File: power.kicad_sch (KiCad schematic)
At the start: 20 parts, among them U2 BQ25176J, U3 TPS61201DRC

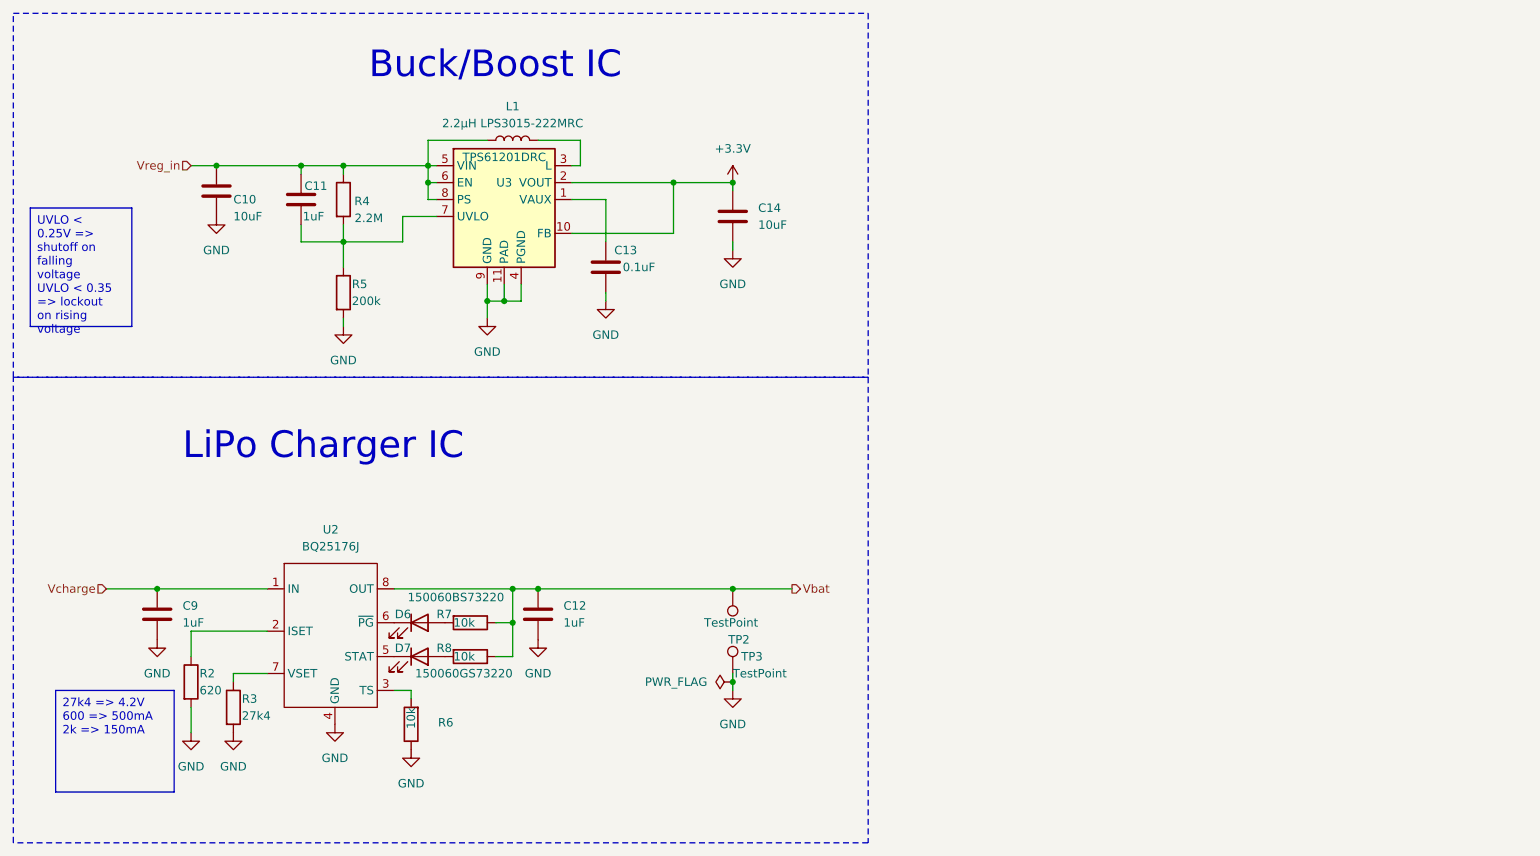
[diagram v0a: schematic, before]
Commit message: update to kicad 9.0 and place Qi-charge IC
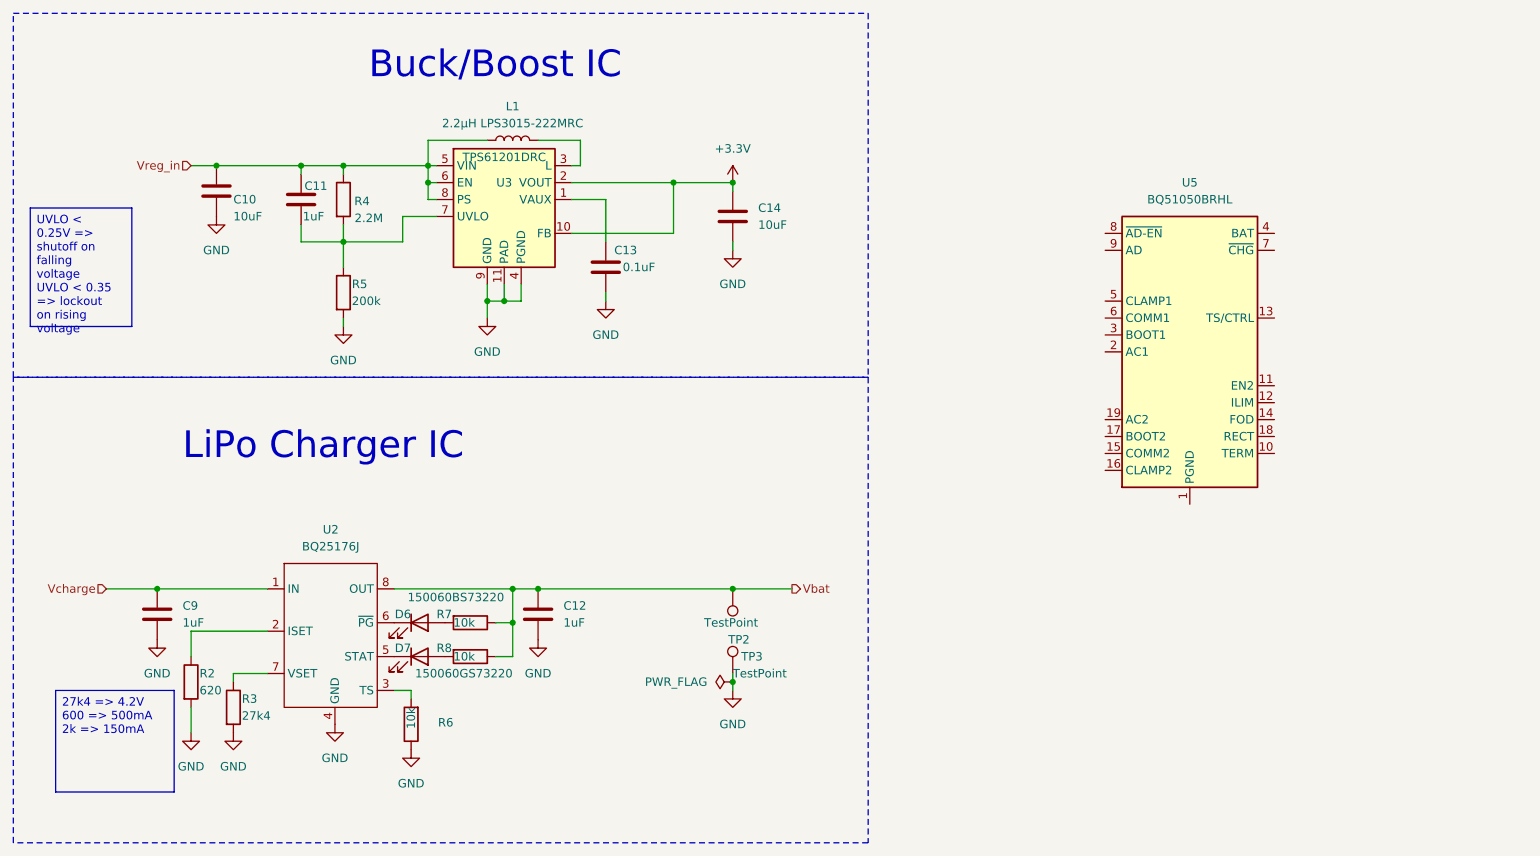
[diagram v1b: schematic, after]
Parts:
- added U5: BQ51050BRHL, Package_DFN_QFN:Texas_VQFN-RHL-20, symbol Battery_Management:BQ51050BRHL
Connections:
- new net: U5.1 (PGND), U5.20 (PGND), U5.21 (PGND)
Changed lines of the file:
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@@
 (kicad_sch
-	(version 20231120)
+	(version 20250114)
 	(generator "eeschema")
-	(generator_version "8.0")
+	(generator_version "9.0")
 	(paper "A4")
+	(rectangle
+		(start 17.78 34.29)
+		(end 146.05 88.9)
+		(stroke
+			(width 0)
+			(type dash_dot)
+		)
+		(fill
+			(type none)
+		)
+	)
+	(rectangle
+		(start 17.78 88.9)
+		(end 146.05 158.75)
+		(stroke
+			(width 0)
+			(type dash_dot)
+		)
+		(fill
+			(type none)
+		)
+	)
+	(text "Buck/Boost IC"
+		(exclude_from_sim no)
+		(at 71.12 44.45 0)
+		(effects
+			(font
+				(size 4 4)
+			)
+			(justify left bottom)
+		)
+	)
+	(text "LiPo Charger IC"
+		(exclude_from_sim no)
+		(at 43.18 101.6 0)
+		(effects
+			(font
+				(size 4 4)
+			)
+			(justify left bottom)
+		)
+	)
+	(text_box "27k4 => 4.2V\n600 => 500mA\n2k => 150mA"
+		(exclude_from_sim no)
+		(at 24.13 135.89 0)
+		(size 17.78 15.24)
+		(margins 0.9525 0.9525 0.9525 0.9525)
+		(stroke
+			(width 0)
+			(type default)
+		)
+		(fill
+			(type none)
+		)
+		(effects
+			(font
+				(size 1.27 1.27)
+			)
+			(justify left top)
+		)
+	)
+	(text_box "UVLO < 0.25V => shutoff on falling voltage\nUVLO < 0.35 => lockout on rising voltage"
+		(exclude_from_sim no)
+		(at 20.32 63.5 0)
+		(size 15.24 17.78)
+		(margins 0.9525 0.9525 0.9525 0.9525)
+		(stroke
+			(width 0)
+			(type default)
+		)
+		(fill
+			(type none)
+		)
+		(effects
+			(font
+				(size 1.27 1.27)
+			)
+			(justify left top)
+		)
+	)
 	(junction
 		(at 48.26 57.15)
@@
 		)
 	)
-	(rectangle
-		(start 17.78 34.29)
-		(end 146.05 88.9)
-		(stroke
-			(width 0)
-			(type dash_dot)
-		)
-		(fill
-			(type none)
-		)
-	)
-	(rectangle
-		(start 17.78 88.9)
-		(end 146.05 158.75)
-		(stroke
-			(width 0)
-			(type dash_dot)
-		)
-		(fill
-			(type none)
-		)
-	)
-	(text_box "27k4 => 4.2V\n600 => 500mA\n2k => 150mA"
-		(exclude_from_sim no)
-		(at 24.13 135.89 0)
-		(size 17.78 15.24)
-		(stroke
-			(width 0)
-			(type default)
-		)
-		(fill
-			(type none)
-		)
-		(effects
-			(font
-				(size 1.27 1.27)
-			)
-			(justify left top)
-		)
-	)
-	(text_box "UVLO < 0.25V => shutoff on falling voltage\nUVLO < 0.35 => lockout on rising voltage"
-		(exclude_from_sim no)
-		(at 20.32 63.5 0)
-		(size 15.24 17.78)
-		(stroke
-			(width 0)
-			(type default)
-		)
-		(fill
-			(type none)
-		)
-		(effects
-			(font
-				(size 1.27 1.27)
-			)
-			(justify left top)
-		)
-	)
-	(text "Buck/Boost IC"
-		(exclude_from_sim no)
-		(at 71.12 44.45 0)
-		(effects
-			(font
-				(size 4 4)
-			)
-			(justify left bottom)
-		)
-	)
-	(text "LiPo Charger IC"
-		(exclude_from_sim no)
-		(at 43.18 101.6 0)
-		(effects
-			(font
-				(size 4 4)
-			)
-			(justify left bottom)
-		)
-	)
 	(hierarchical_label "Vcharge"
 		(shape input)
@@
 					(unit 1)
 				)
+			)
+		)
+	)
+	(symbol
+		(lib_id "Battery_Management:BQ51050BRHL")
+		(at 194.31 85.09 0)
+		(unit 1)
+		(exclude_from_sim no)
+		(in_bom yes)
+		(on_board yes)
+		(dnp no)
+		(fields_autoplaced yes)
+		(property "Reference" "U5"
+			(at 194.31 59.69 0)
+			(effects
+				(font
+					(size 1.27 1.27)
+				)
+			)
+		)
+		(property "Value" "BQ51050BRHL"
+			(at 194.31 62.23 0)
+			(effects
+				(font
+					(size 1.27 1.27)
+				)
+			)
+		)
+		(property "Footprint" "Package_DFN_QFN:Texas_VQFN-RHL-20"
+			(at 214.63 106.68 0)
+			(effects
+				(font
+					(size 1.27 1.27)
+				)
+				(hide yes)
+			)
+		)
+		(property "Datasheet" "http://www.ti.com/lit/ds/symlink/bq51050b.pdf"
+			(at 194.31 85.09 0)
+			(effects
+				(font
+					(size 1.27 1.27)
+				)
+				(hide yes)
+			)
+		)
+		(property "Description" "Qi v1.2, Wireless Power Receiver and Battery Charger, Vout 4.2V, VQFN-20"
+			(at 194.31 85.09 0)
+			(effects
+				(font
+					(size 1.27 1.27)
+				)
+				(hide yes)
+			)
+		)
+		(pin "6"
+		)
+		(pin "8"
+		)
+		(pin "13"
+		)
+		(pin "5"
+		)
+		(pin "17"
+		)
+		(pin "11"
+		)
+		(pin "7"
+		)
+		(pin "15"
+		)
+		(pin "14"
+		)
+		(pin "1"
+		)
+		(pin "9"
+		)
+		(pin "10"
+		)
+		(pin "16"
+		)
+		(pin "20"
+		)
+		(pin "3"
+		)
+		(pin "12"
+		)
+		(pin "2"
+		)
+		(pin "4"
+		)
+		(pin "18"
+		)
+		(pin "21"
+		)
+		(pin "19"
+		)
+		(instances
+			(project ""
+				(path "/a4ffe097-37ef-4e19-a91a-ae57f4a5aad1/06d9cd17-cb19-4cdd-8e67-c41d1b4a676e"
+					(reference "U5")
+					(unit 1)
+				)

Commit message: continue Qi-Charge circuit
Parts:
- added C16, C21: 10nF 25V, Capacitor_SMD:C_0805_2012Metric, symbol Device:C_Small
- added C17, C20: 22nF 25V, Capacitor_SMD:C_0805_2012Metric, symbol Device:C_Small
- added C18, C19: 470nF 25V, Capacitor_SMD:C_0805_2012Metric, symbol Device:C_Small
- added C22: CS, Capacitor_SMD:C_0805_2012Metric, symbol Device:C_Small
- added C23: CP, Capacitor_SMD:C_0805_2012Metric, symbol Device:C_Small
- added C24: 1uF, Capacitor_SMD:C_0805_2012Metric, symbol Device:C
- added C25, C27: 10uF 25V, Capacitor_SMD:C_0805_2012Metric, symbol Device:C_Small
- added C26: 0.1uF 25V, Capacitor_SMD:C_0805_2012Metric, symbol Device:C_Small
- added D8: 150060GS73220, LED_SMD:LED_0603_1608Metric_Pad1.05x0.95mm_HandSolder, symbol Device:LED
- added L2: 8.3uH 160mOhm, symbol Device:L
- added R17, R18: 10k, Resistor_SMD:R_0805_2012Metric, symbol Device:R
- added R19: 2k4, Resistor_SMD:R_0805_2012Metric, symbol Device:R_Small
- added R20: 330, Resistor_SMD:R_0805_2012Metric, symbol Device:R_Small
- added R21: 300, Resistor_SMD:R_0805_2012Metric, symbol Device:R_Small
- added R22: 42k, Resistor_SMD:R_0805_2012Metric, symbol Device:R_Small
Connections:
- net GND: now also U5.1 (PGND), U5.20 (PGND), U5.21 (PGND), U5.9 (AD), C24.2, C25.2, C26.2, C27.2, R18.1, R19.1, R21.1
- net Vbat: now also U5.4 (BAT), C24.1, R17.1
- net at U5.10 (TERM): now also R19.2
- net at U5.12 (ILIM): now also R20.2
- net at U5.13 (TS/CTRL): now also R18.2
- net at U5.14 (FOD): now also R20.1, R21.2, R22.1
- net at U5.15 (COMM2): now also C20.2
- net at U5.16 (CLAMP2): now also C19.2
- net at U5.17 (BOOT2): now also C21.2
- net at U5.18 (RECT): now also C25.1, C26.1, C27.1, R22.2
- net at U5.19 (AC2): now also C19.1, C20.1, C21.1, C23.1, L2.1
- net at U5.2 (AC1): now also C16.1, C17.1, C18.1, C22.2, C23.2
- net at U5.3 (BOOT1): now also C16.2
- net at U5.5 (CLAMP1): now also C18.2
- net at U5.6 (COMM1): now also C17.2
- net at U5.7 (~{CHG}): now also D8.1 (K)
- new net: D8.2 (A), R17.2
- new net: C22.1, L2.2
- no-connect marks 0 -> 1

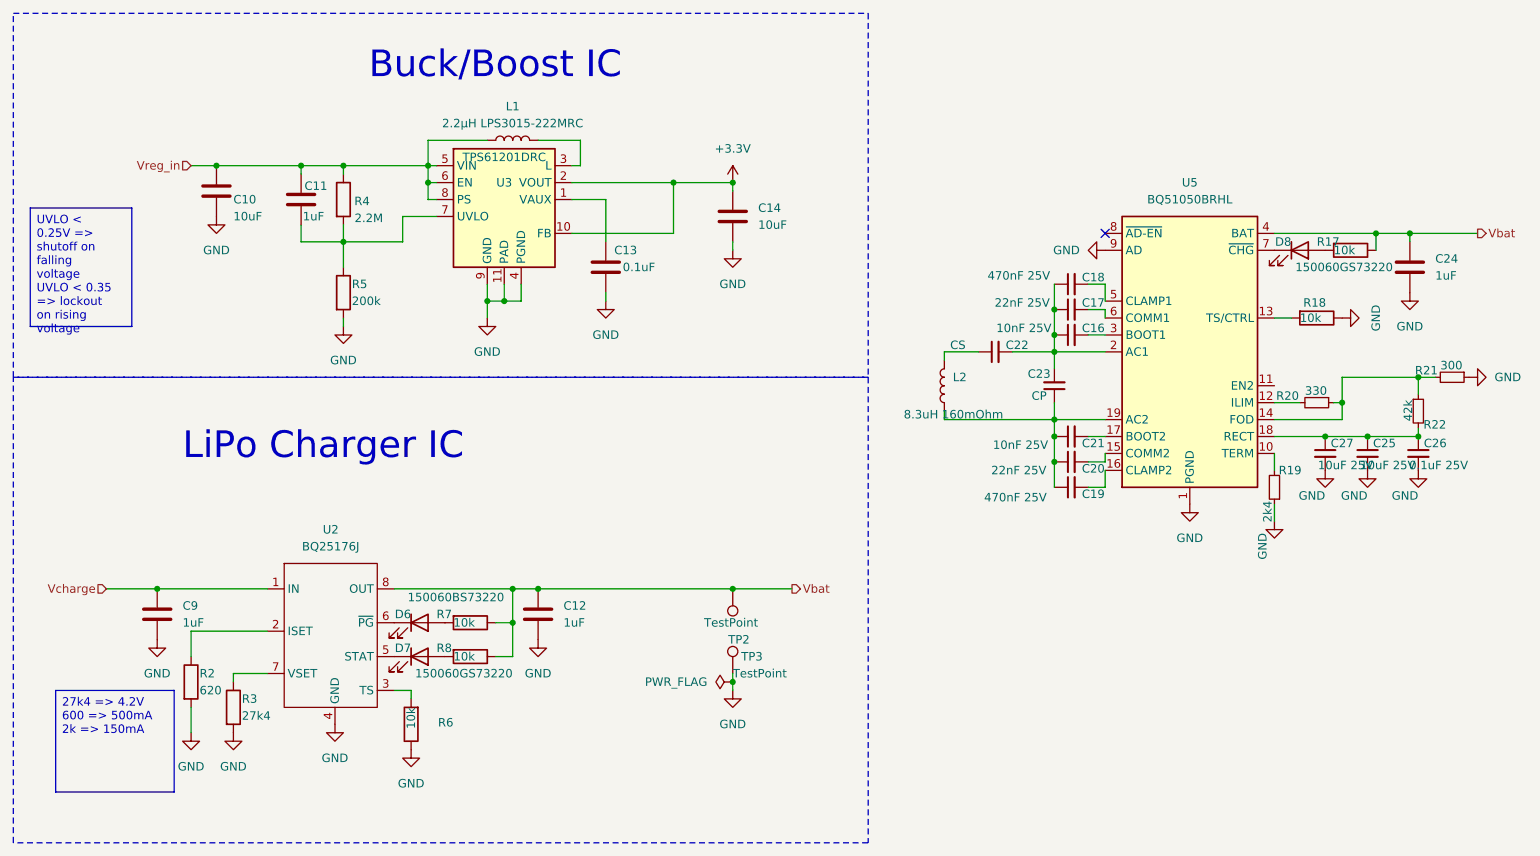
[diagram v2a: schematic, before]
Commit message: implement initial power latching idea
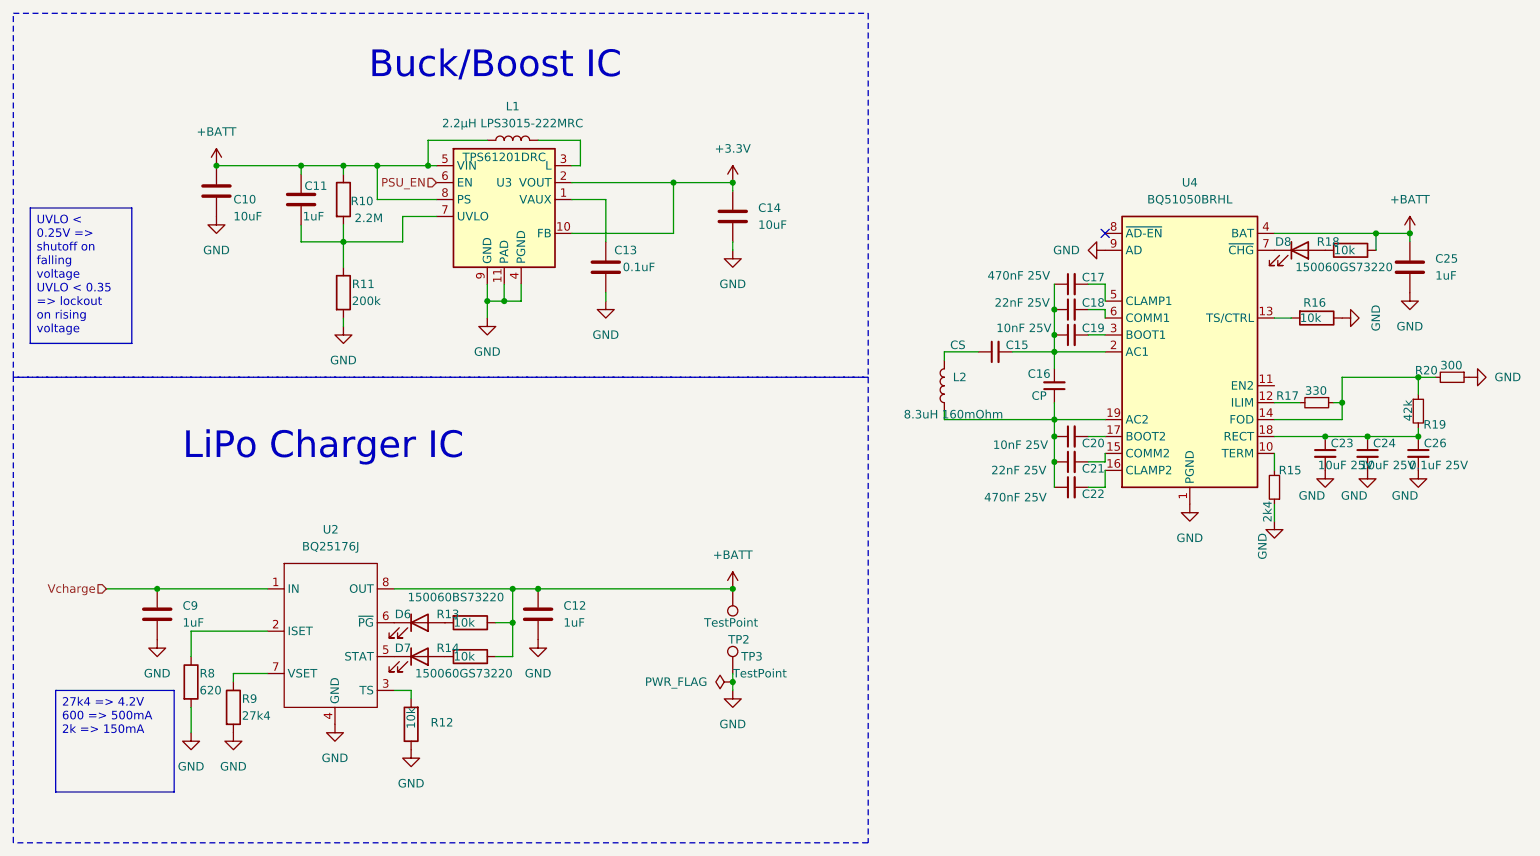
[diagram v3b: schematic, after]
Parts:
- renumbered C22 to C15, C23 to C16, C18 to C17, C17 to C18, C16 to C19, C21 to C20, C20 to C21, C19 to C22, C27 to C23, C25 to C24, C24 to C25, R4 to R10, R5 to R11, R6 to R12, R7 to R13, R8 to R14, R19 to R15, R18 to R16, R20 to R17, R17 to R18, R22 to R19, R21 to R20, R2 to R8, R3 to R9, U5 to U4
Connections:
- net Vbat renamed +BATT
- net +BATT: now also C10.1, C11.1, L1.1, R10.1, U3.5 (VIN), U3.8 (PS)
- removed net Vreg_in: C10.1, C11.1, L1.1, R10.1, U3.5 (VIN), U3.6 (EN), U3.8 (PS)
- new net PSU_EN: U3.6 (EN)

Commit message: continue Qi-Charger work
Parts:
- C15, C16, C17, C18, C19, C20, C21, C22, C23, C24, C26: footprint Capacitor_SMD:C_0805_2012Metric -> Capacitor_SMD:C_0402_1005Metric
- L2: footprint (none) -> Inductor_SMD:L_0603_1608Metric
- R15, R17, R19, R20: footprint Resistor_SMD:R_0805_2012Metric -> Resistor_SMD:R_0603_1608Metric
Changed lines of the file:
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@@
 			)
 		)
-		(property "Footprint" "Capacitor_SMD:C_0805_2012Metric"
+		(property "Footprint" "Capacitor_SMD:C_0402_1005Metric"
 			(at 176.53 101.6 0)
 			(effects
@@
 			)
 		)
-		(property "Footprint" "Capacitor_SMD:C_0805_2012Metric"
+		(property "Footprint" "Capacitor_SMD:C_0402_1005Metric"
 			(at 176.53 78.74 0)
 			(effects
@@
 			)
 		)
-		(property "Footprint" "Capacitor_SMD:C_0805_2012Metric"
+		(property "Footprint" "Capacitor_SMD:C_0402_1005Metric"
 			(at 176.53 82.55 0)
 			(effects
@@
 			)
 		)
-		(property "Footprint" "Capacitor_SMD:C_0805_2012Metric"
+		(property "Footprint" "Capacitor_SMD:C_0402_1005Metric"
 			(at 214.63 100.33 0)
 			(effects
@@
 			)
 		)
-		(property "Footprint" "Resistor_SMD:R_0805_2012Metric"
+		(property "Footprint" "Resistor_SMD:R_0603_1608Metric"
 			(at 207.01 105.41 0)
 			(effects
@@
 			)
 		)
-		(property "Footprint" "Capacitor_SMD:C_0805_2012Metric"
+		(property "Footprint" "Capacitor_SMD:C_0402_1005Metric"
 			(at 220.98 100.33 0)
 			(effects
@@
 			)
 		)
-		(property "Footprint" "Capacitor_SMD:C_0805_2012Metric"
+		(property "Footprint" "Capacitor_SMD:C_0402_1005Metric"
 			(at 173.99 90.17 0)
 			(effects
@@
 			)
 		)
-		(property "Footprint" "Capacitor_SMD:C_0805_2012Metric"
+		(property "Footprint" "Capacitor_SMD:C_0402_1005Metric"
 			(at 165.1 85.09 0)
 			(effects
@@
 			)
 		)
-		(property "Footprint" "Capacitor_SMD:C_0805_2012Metric"
+		(property "Footprint" "Capacitor_SMD:C_0402_1005Metric"
 			(at 176.53 105.41 0)
 			(effects
@@
 			)
 		)
-		(property "Footprint" "Capacitor_SMD:C_0805_2012Metric"
+		(property "Footprint" "Capacitor_SMD:C_0402_1005Metric"
 			(at 228.6 100.33 0)
 			(effects
@@
 			)
 		)
-		(property "Footprint" "Capacitor_SMD:C_0805_2012Metric"
+		(property "Footprint" "Capacitor_SMD:C_0402_1005Metric"
 			(at 176.53 74.93 0)
 			(effects
@@
 			)
 		)
-		(property "Footprint" "Capacitor_SMD:C_0805_2012Metric"
+		(property "Footprint" "Capacitor_SMD:C_0402_1005Metric"
 			(at 176.53 97.79 0)
 			(effects
@@
 			)
 		)
-		(property "Footprint" ""
+		(property "Footprint" "Inductor_SMD:L_0603_1608Metric"
 			(at 157.48 90.17 0)
 			(effects
@@
 			)
 		)
-		(property "Footprint" "Resistor_SMD:R_0805_2012Metric"
+		(property "Footprint" "Resistor_SMD:R_0603_1608Metric"
 			(at 228.6 93.98 0)
 			(effects
@@
 			)
 		)
-		(property "Footprint" "Resistor_SMD:R_0805_2012Metric"
+		(property "Footprint" "Resistor_SMD:R_0603_1608Metric"
 			(at 213.36 92.71 0)
 			(effects
@@
 			)
 		)
-		(property "Footprint" "Resistor_SMD:R_0805_2012Metric"
+		(property "Footprint" "Resistor_SMD:R_0603_1608Metric"
 			(at 233.68 88.9 0)
 			(effects
